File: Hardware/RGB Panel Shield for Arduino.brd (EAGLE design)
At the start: 53.3 x 59.7 mm, 121 parts, among them J7 Screw Terminal, J8 SparkFun Panel, U1 ARDUINO UNO

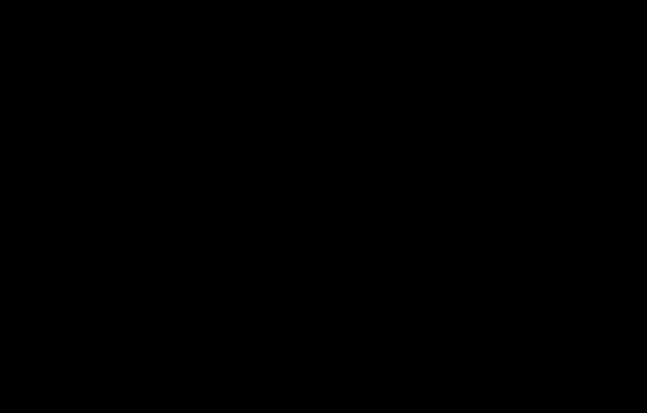
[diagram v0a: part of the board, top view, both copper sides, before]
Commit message: Readme fix
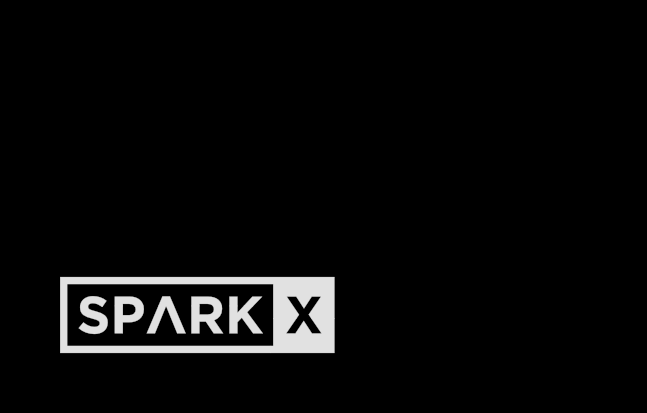
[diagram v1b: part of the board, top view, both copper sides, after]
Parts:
- added U$91: SPARKX-LOGO4, SparkX:SPARKX-MEDIUM
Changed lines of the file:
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@@
 <layer number="44" name="Drills" color="7" fill="1" visible="no" active="yes"/>
 <layer number="45" name="Holes" color="7" fill="1" visible="yes" active="yes"/>
-<layer number="46" name="Milling" color="3" fill="1" visible="yes" active="yes"/>
+<layer number="46" name="Milling" color="3" fill="1" visible="no" active="yes"/>
 <layer number="47" name="Measures" color="7" fill="1" visible="no" active="yes"/>
 <layer number="48" name="Document" color="7" fill="1" visible="no" active="yes"/>
@@
 <element name="U$2" library="SparkX" package="SPARKX-MEDIUM" value="" x="8.89" y="3.81"/>
 <element name="U$128" library="SparkX" package="SPARKX-MEDIUM" value="" x="8.89" y="3.81" rot="MR0"/>
+<element name="U$91" library="SparkX" package="SPARKX-MEDIUM" value="SPARKX-LOGO4" x="-24.13" y="-30.48"/>
 </elements>
 <signals>
